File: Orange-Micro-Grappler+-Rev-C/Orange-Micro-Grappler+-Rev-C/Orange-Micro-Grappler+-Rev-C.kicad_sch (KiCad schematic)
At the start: 23 parts, among them J1 Conn_02x13, J2 AppleIIBus, U1 74LS00, U10 74LS374, U11 74LS373, U2 74LS279, U3 74LS02, U4 74LS00, U5 74LS74, U6 74LS00, U7 74LS08, U8 74LS30, U9 27C32

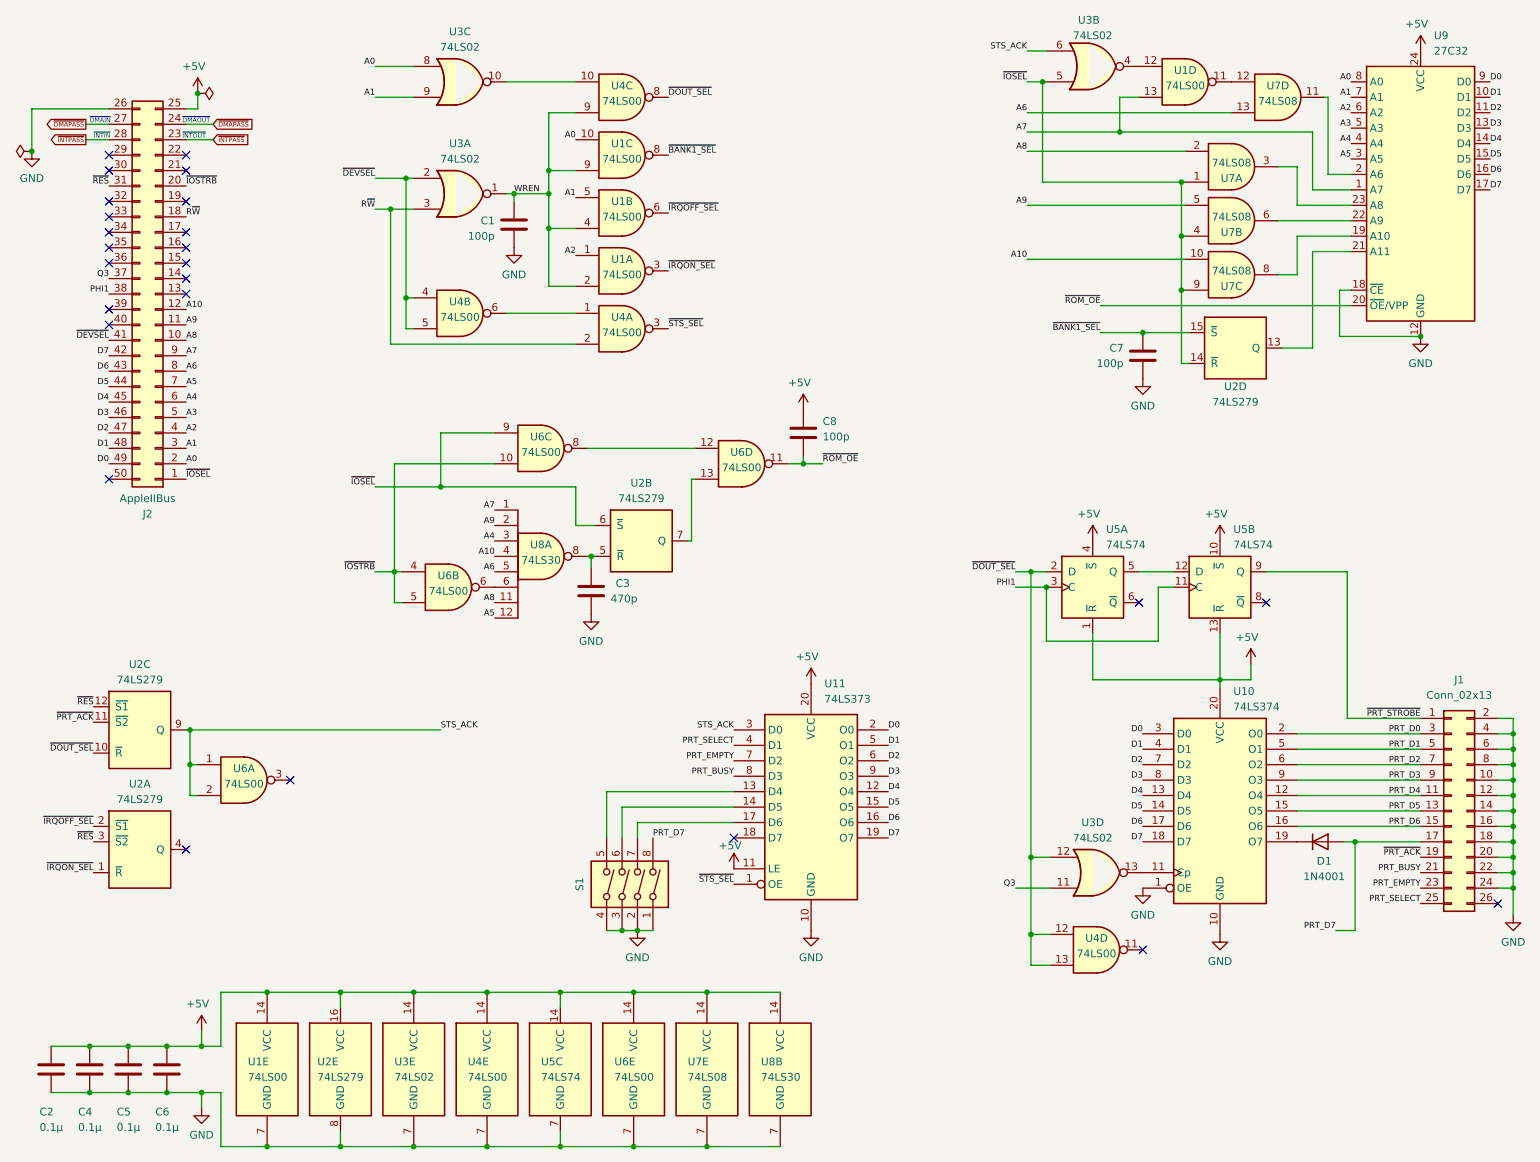
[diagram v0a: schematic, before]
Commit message: Update Grappler projects to kicad8 and the shared symbol library
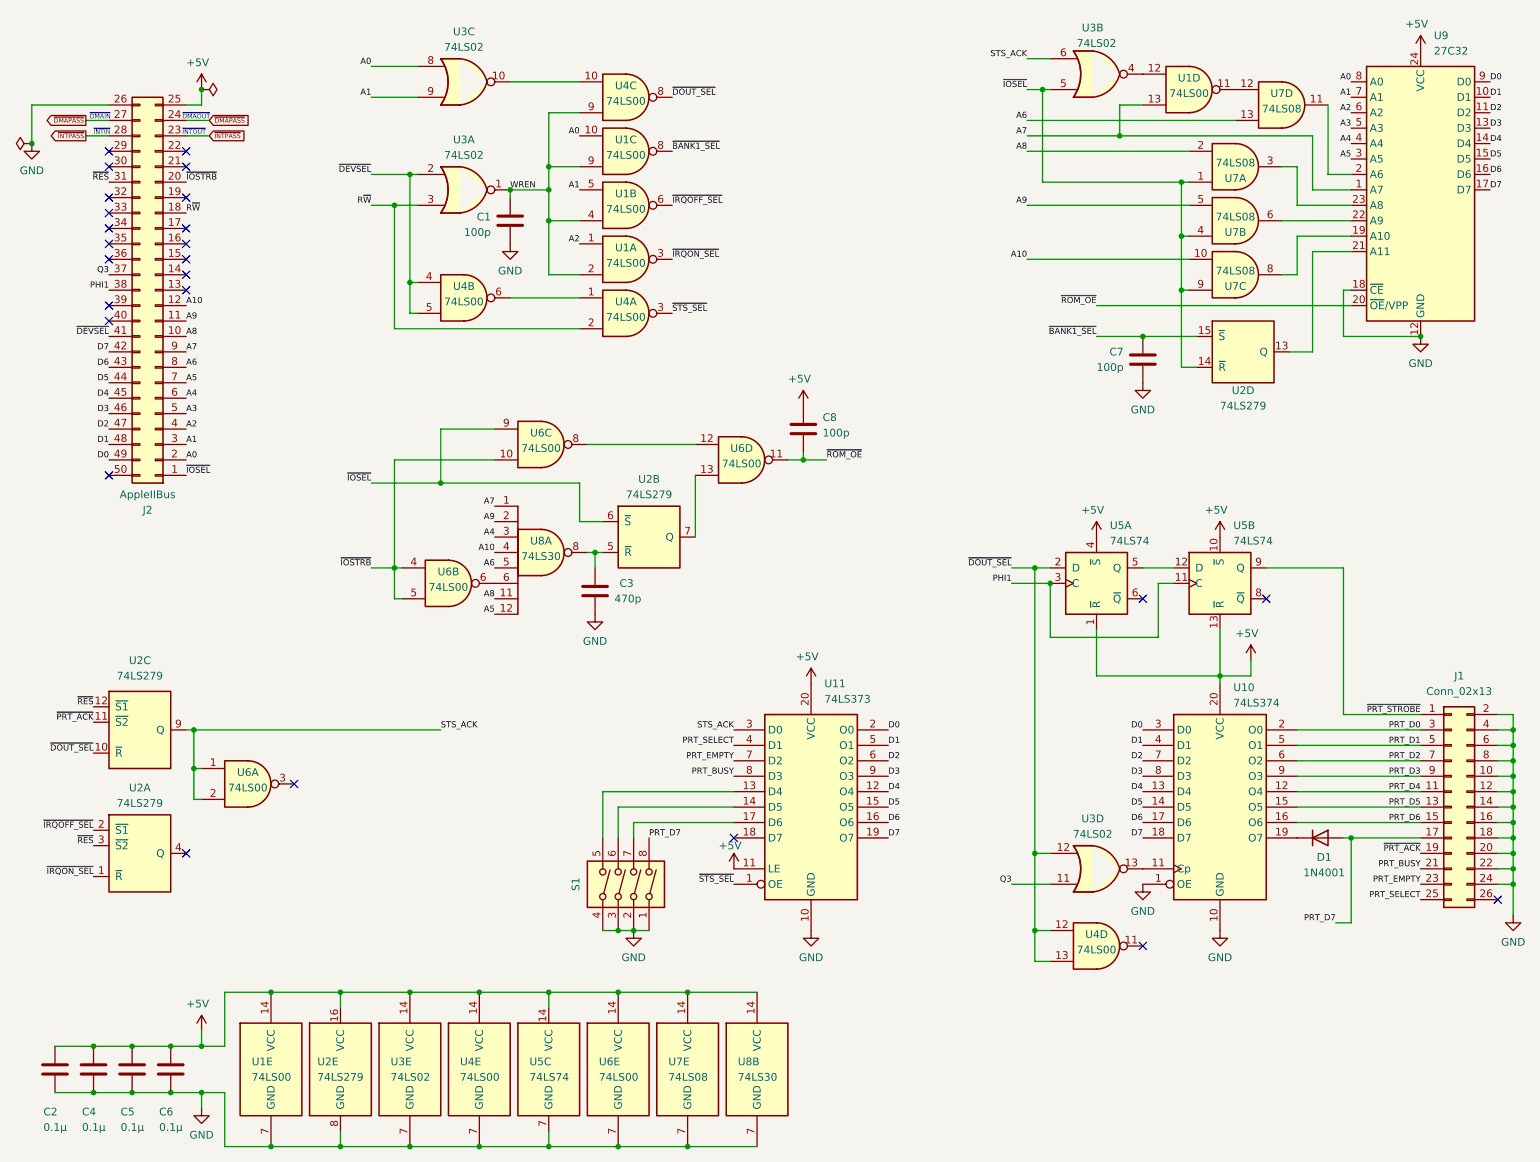
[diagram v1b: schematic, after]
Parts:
- U2: symbol Logic:74LS279 -> Logic_Legacy:74LS279
- U9: symbol Memory:27C32 -> Memory_Legacy:27C32
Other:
- moved on the sheet: C1, C2, C3, C4, C5, C6, C7, C8, D1, J1, J2, S1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
